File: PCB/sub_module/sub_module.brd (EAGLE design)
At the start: 73.5 x 28.8 mm, 11 parts, among them J1 J7MM, J2 J7MM, X1 DCJACK-MJ179P-R

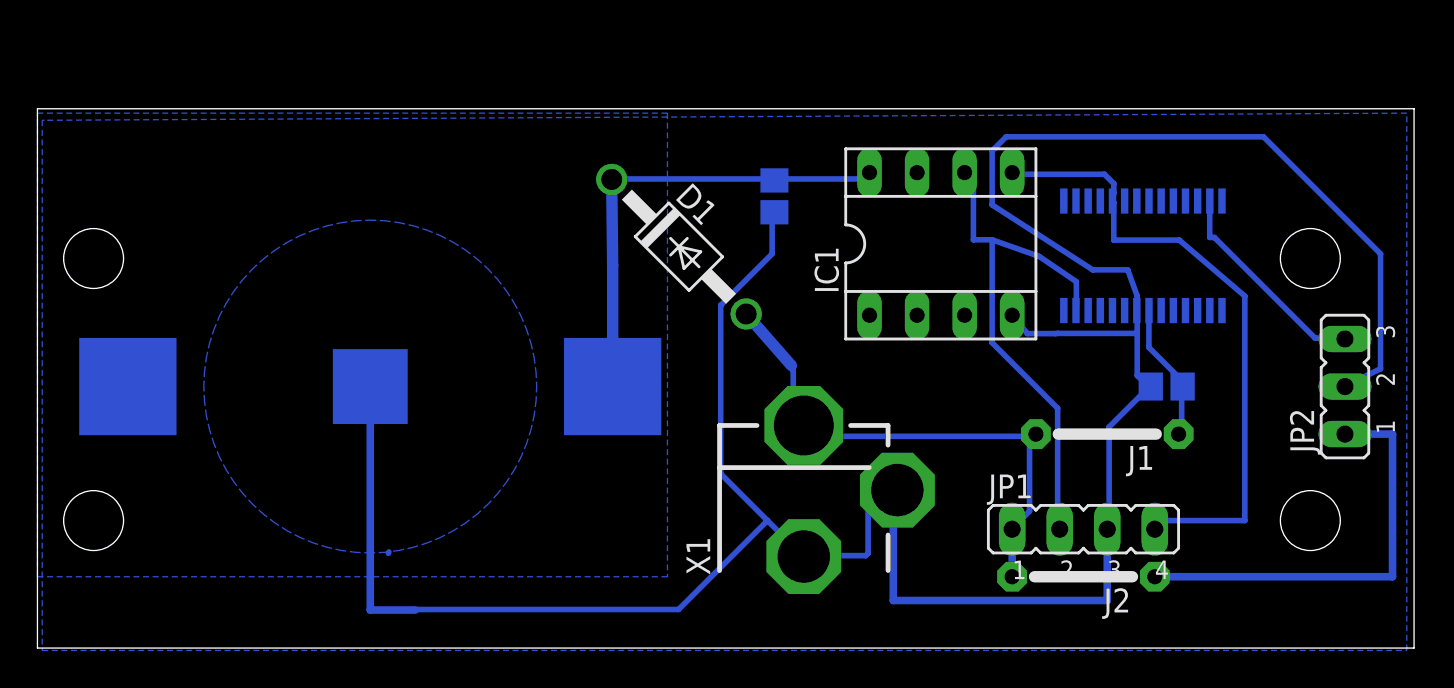
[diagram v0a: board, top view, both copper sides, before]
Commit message: sub_moduleを改良
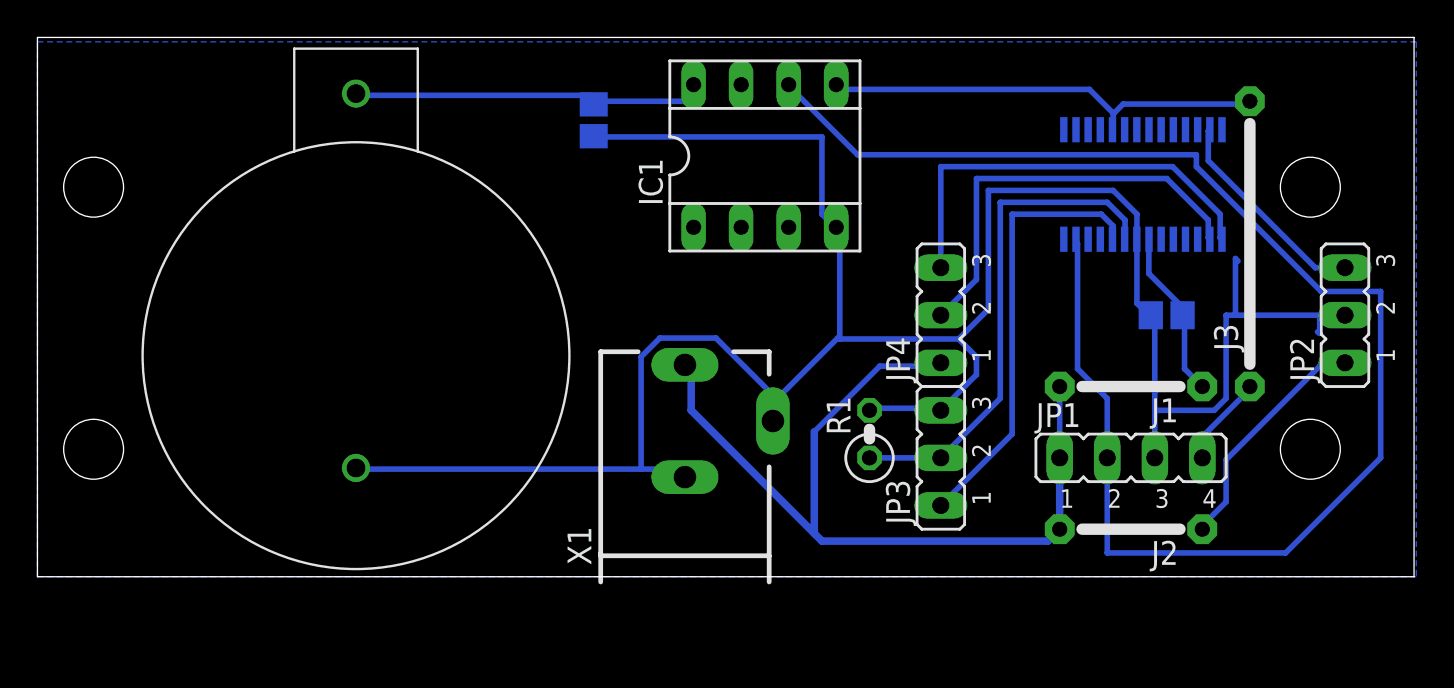
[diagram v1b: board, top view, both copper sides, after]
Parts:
- removed D1: BAT49, diode:DO41-10
- added J3: J15MM, jumper:15
- added JP3, JP4: (no value), jumper:JP2
- added R1: 4.7k, rcl:0207/2V
- U$1: value CR2032-HOLDER -> CR2032-HOLDER2; device CR2032-holder:CR2032-HOLDER -> CR2032-holder:CR2032-HOLDER2
- X1: value DCJACK-MJ179P-R -> DCJACK-PJ102-R; device dcjack:MJ-179P-R -> dcjack:PJ-102-R
- moved IC1 10.5 mm to (38.9, 22.5)
- moved C2 10.5 mm to (29.7, 24.4)
- moved X1 6.84 mm to (34.6, 7.62)
- moved JP1 4.58 mm to (58.4, 6.35)
- moved C1 3.81 mm to (60.3, 14.0)
- moved JP2 3.81 mm to (69.8, 14.0)
- moved U$2 3.81 mm to (59.1, 21.0)
- moved J2 3.59 mm to (58.4, 2.54)
- moved J1 2.84 mm to (58.4, 10.2)
- moved U$1 1.82 mm to (17.0, 11.8), flipped to the top
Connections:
- new net N$10: JP3.1, U$2.24
- new net N$4: JP4.3, U$2.15
- new net N$7: JP4.2, U$2.16
- new net N$8: J3.1, JP1.4
- new net N$9: JP3.2, R1.1, U$2.23
- net GND: now also JP3.3, R1.2
- net N$2: now also J3.2; no longer JP1.4
- net VCC: now also U$1.+3V; no longer D1.C, U$1.3VR
- net VDD: now also JP4.1; no longer D1.A
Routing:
- net N$1: track 28.5 -> 79.6 mm
- net N$9: track 0.00 -> 26.9 mm
- net N$10: track 0.00 -> 23.5 mm
- net N$4: track 0.00 -> 22.8 mm
- net N$7: track 0.00 -> 22.5 mm
- net GND: track 152.1 -> 130.0 mm
- net VDD: track 28.3 -> 47.0 mm
- net N$5: track 22.9 -> 12.8 mm
- net N$2: track 33.8 -> 24.0 mm
- net VCC: track 25.2 -> 19.3 mm
- net N$8: track 0.00 -> 4.85 mm
- net N$3: track 7.45 -> 9.24 mm
- removed copper zone on layer 16, net VCC
